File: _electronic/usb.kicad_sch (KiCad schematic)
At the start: 8 parts

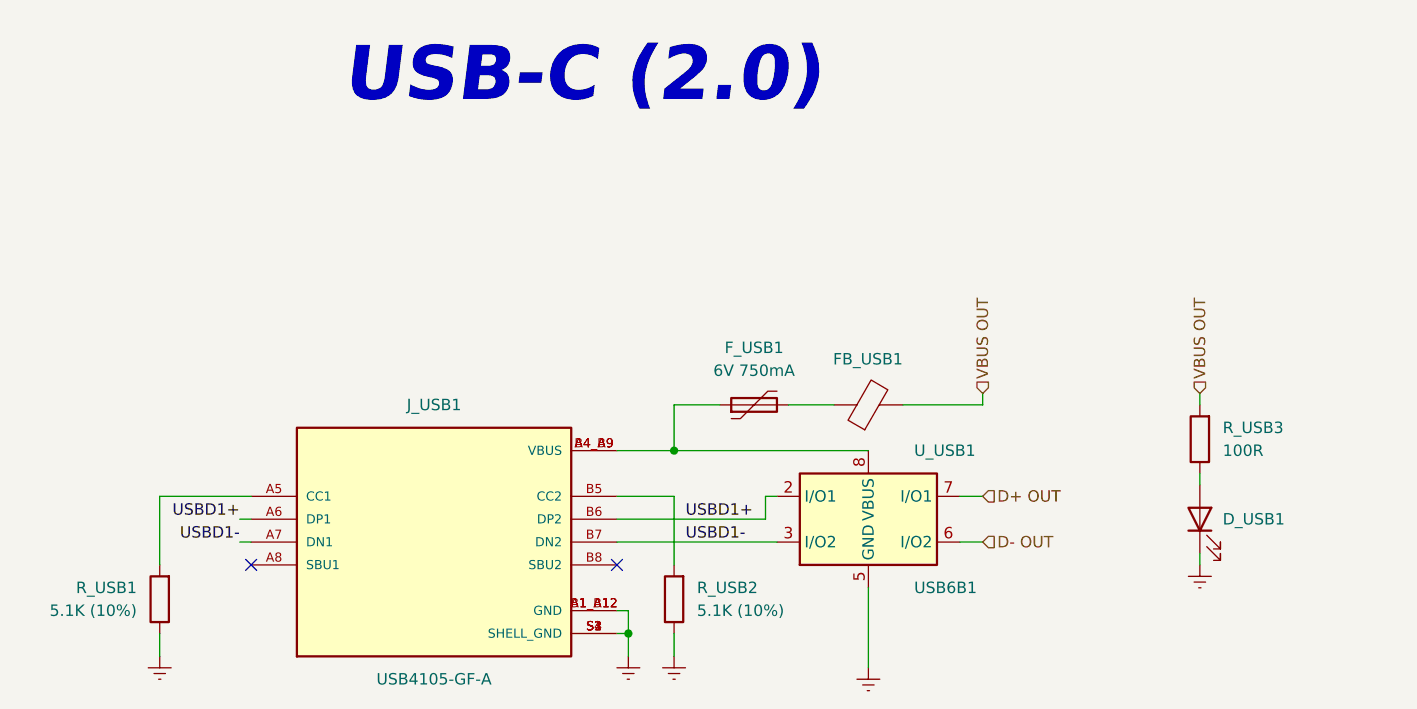
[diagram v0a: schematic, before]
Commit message: led resistor revision, b.o.m. and pcb anotation
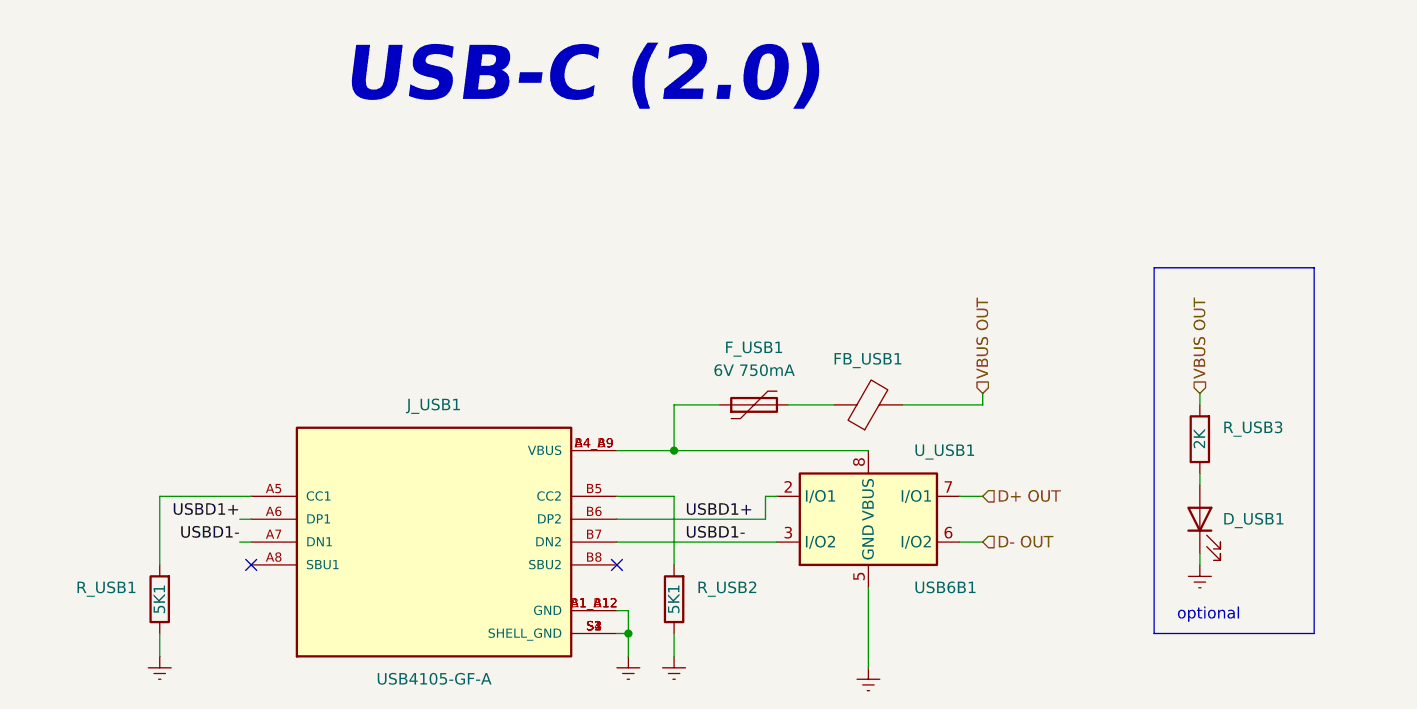
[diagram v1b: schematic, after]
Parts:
- R_USB1, R_USB2: value 5.1K (10%) -> 5K1; # CR0603-FX-5101ELF -> ERJ-3EKF5101V
- R_USB3: value 100R -> 2K; # CHP0603AFX-1000ELF -> ERJ-3EKF2001V
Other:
- note added: "optional"
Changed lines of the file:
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@@
+    (stroke (width 0) (type default) (color 0 0 0 0))
+  )
+  (polyline (pts (xy 201.93 72.39) (xy 219.71 72.39))
     (stroke (width 0) (type default) (color 0 0 0 0))
   )
@@
     (stroke (width 0) (type default) (color 0 0 0 0))
   )
+  (polyline (pts (xy 219.71 72.39) (xy 219.71 113.03))
+    (stroke (width 0) (type default) (color 0 0 0 0))
+  )
   (wire (pts (xy 91.44 97.79) (xy 91.44 105.41))
     (stroke (width 0) (type default) (color 0 0 0 0))
@@
     (stroke (width 0) (type default) (color 0 0 0 0))
   )
+  (polyline (pts (xy 219.71 113.03) (xy 201.93 113.03))
+    (stroke (width 0) (type default) (color 0 0 0 0))
+  )
   (wire (pts (xy 148.59 87.63) (xy 148.59 92.71))
     (stroke (width 0) (type default) (color 0 0 0 0))
@@
   )
   (wire (pts (xy 100.33 102.87) (xy 101.6 102.87))
+    (stroke (width 0) (type default) (color 0 0 0 0))
+  )
+  (polyline (pts (xy 201.93 72.39) (xy 201.93 113.03))
     (stroke (width 0) (type default) (color 0 0 0 0))
   )
@@
     (effects (font (size 6 6) (thickness 0.6) bold italic) (justify left bottom))
   )
+  (text "optional" (at 204.47 111.76 0)
+    (effects (font (size 1.27 1.27)) (justify left bottom))
+  )
   (label "USBD1-" (at 149.86 102.87 0)
     (effects (font (size 1.27 1.27)) (justify left bottom))
@@
       (effects (font (size 1.27 1.27)) (justify right))
     )
-    (property "Value" "5.1K (10%)" (id 1) (at 151.13 110.49 0)
-      (effects (font (size 1.27 1.27)) (justify right))
-    )
+    (property "Value" "5K1" (id 1) (at 148.59 109.22 90))
     (property "Footprint" "Resistor_SMD:R_0603_1608Metric_Pad0.98x0.95mm_HandSolder" (id 2) (at 150.368 109.22 90)
       (effects (font (size 1.27 1.27)) hide)
@@
       (effects (font (size 1.27 1.27)) hide)
     )
-    (property "#" "CR0603-FX-5101ELF" (id 4) (at 151.13 111.76 0)
+    (property "#" "ERJ-3EKF5101V" (id 4) (at 151.13 111.76 0)
       (effects (font (size 1.27 1.27) italic) (justify right) hide)
     )
@@
       (effects (font (size 1.27 1.27)) (justify right))
     )
-    (property "Value" "100R" (id 1) (at 209.55 92.71 0)
-      (effects (font (size 1.27 1.27)) (justify right))
-    )
+    (property "Value" "2K" (id 1) (at 207.01 91.44 90))
     (property "Footprint" "Resistor_SMD:R_0603_1608Metric_Pad0.98x0.95mm_HandSolder" (id 2) (at 208.788 91.44 90)
       (effects (font (size 1.27 1.27)) hide)
@@
       (effects (font (size 1.27 1.27)) hide)
     )
-    (property "#" "CHP0603AFX-1000ELF" (id 4) (at 224.79 90.17 0)
+    (property "#" "ERJ-3EKF2001V" (id 4) (at 224.79 90.17 0)
       (effects (font (size 1.27 1.27) italic) (justify left) hide)
     )
@@
       (effects (font (size 1.27 1.27)) (justify left))
     )
-    (property "Value" "5.1K (10%)" (id 1) (at 88.9 110.49 0)
-      (effects (font (size 1.27 1.27)) (justify left))
-    )
+    (property "Value" "5K1" (id 1) (at 91.44 109.22 90))
     (property "Footprint" "Resistor_SMD:R_0603_1608Metric_Pad0.98x0.95mm_HandSolder" (id 2) (at 93.218 109.22 90)
       (effects (font (size 1.27 1.27)) hide)
@@
       (effects (font (size 1.27 1.27)) hide)
     )
-    (property "#" "CR0603-FX-5101ELF" (id 4) (at 88.9 111.76 0)
+    (property "#" "ERJ-3EKF5101V" (id 4) (at 88.9 111.76 0)
       (effects (font (size 1.27 1.27) italic) (justify left) hide)
     )

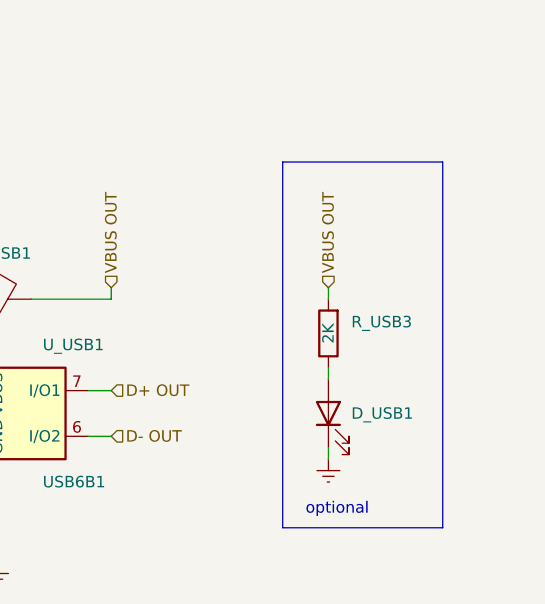
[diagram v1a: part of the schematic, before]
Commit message: schematics and pcb cleanup
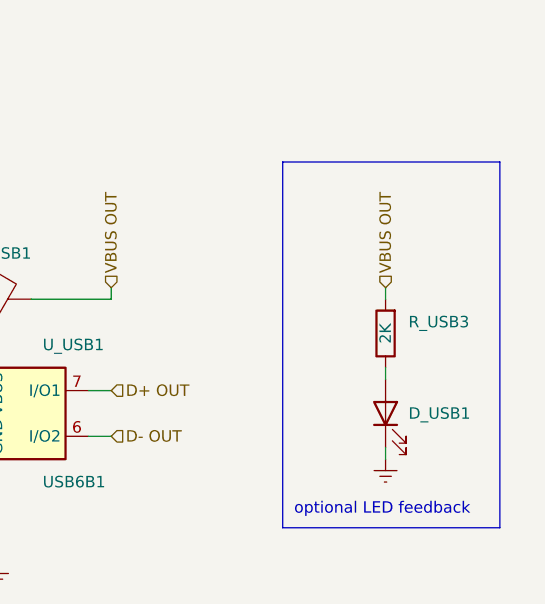
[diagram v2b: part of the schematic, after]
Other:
- note added: "optional LED feedback"
- note removed: "optional"
- title: E-TKT -> E-TKT v1.0
- moved on the sheet: D_USB1, R_USB3
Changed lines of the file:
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@@
   (paper "A4")
   (title_block
-    (title "E-TKT")
-    (date "2022-07-21")
-    (rev "3")
+    (title "E-TKT v1.0")
+    (date "2022-09-29")
+    (rev "4")
     (company "Andrei Speridiao")
   )
@@
     (stroke (width 0) (type default) (color 0 0 0 0))
   )
-  (polyline (pts (xy 201.93 72.39) (xy 219.71 72.39))
+  (polyline (pts (xy 201.93 72.39) (xy 226.06 72.39))
     (stroke (width 0) (type default) (color 0 0 0 0))
   )
@@
     (stroke (width 0) (type default) (color 0 0 0 0))
   )
-  (wire (pts (xy 207.01 104.14) (xy 207.01 105.41))
+  (wire (pts (xy 213.36 104.14) (xy 213.36 105.41))
     (stroke (width 0) (type default) (color 0 0 0 0))
   )
@@
     (stroke (width 0) (type default) (color 0 0 0 0))
   )
-  (polyline (pts (xy 219.71 72.39) (xy 219.71 113.03))
+  (polyline (pts (xy 226.06 72.39) (xy 226.06 113.03))
     (stroke (width 0) (type default) (color 0 0 0 0))
   )
@@
     (stroke (width 0) (type default) (color 0 0 0 0))
   )
-  (polyline (pts (xy 219.71 113.03) (xy 201.93 113.03))
+  (polyline (pts (xy 226.06 113.03) (xy 201.93 113.03))
     (stroke (width 0) (type default) (color 0 0 0 0))
   )
@@
     (stroke (width 0) (type default) (color 0 0 0 0))
   )
-  (wire (pts (xy 207.01 86.36) (xy 207.01 87.63))
+  (wire (pts (xy 213.36 86.36) (xy 213.36 87.63))
     (stroke (width 0) (type default) (color 0 0 0 0))
   )
@@
     (stroke (width 0) (type default) (color 0 0 0 0))
   )
-  (wire (pts (xy 207.01 95.25) (xy 207.01 96.52))
+  (wire (pts (xy 213.36 95.25) (xy 213.36 96.52))
     (stroke (width 0) (type default) (color 0 0 0 0))
   )
@@
     (effects (font (size 6 6) (thickness 0.6) bold italic) (justify left bottom))
   )
-  (text "optional" (at 204.47 111.76 0)
+  (text "optional LED feedback" (at 203.2 111.76 0)
     (effects (font (size 1.27 1.27)) (justify left bottom))
   )
@@
     (effects (font (size 1.27 1.27)) (justify left))
   )
-  (hierarchical_label "VBUS OUT" (shape input) (at 207.01 86.36 90)
+  (hierarchical_label "VBUS OUT" (shape input) (at 213.36 86.36 90)
     (effects (font (size 1.27 1.27)) (justify left))
   )
@@
     (pin "2")
   )
-  (symbol (lib_id "Device:LED") (at 207.01 100.33 90) (unit 1)
+  (symbol (lib_id "Device:LED") (at 213.36 100.33 90) (unit 1)
     (in_bom yes) (on_board yes)
-    (property "Reference" "D_USB1" (id 0) (at 209.55 100.33 90)
+    (property "Reference" "D_USB1" (id 0) (at 215.9 100.33 90)
       (effects (font (size 1.27 1.27)) (justify right))
     )
-    (property "Value" "LED white" (id 1) (at 210.82 102.87 90)
+    (property "Value" "LED white" (id 1) (at 217.17 102.87 90)
       (effects (font (size 1.27 1.27)) (justify right) hide)
     )
-    (property "Footprint" "LED_SMD:LED_0603_1608Metric_Pad1.05x0.95mm_HandSolder" (id 2) (at 207.01 100.33 0)
-      (effects (font (size 1.27 1.27)) hide)
-    )
-    (property "Datasheet" "https://br.mouser.com/datasheet/2/348/smld12-e-1874545.pdf" (id 3) (at 207.01 100.33 0)
-      (effects (font (size 1.27 1.27)) hide)
-    )
-    (property "#" "SMLD12WBN1W1" (id 4) (at 240.03 99.06 90)
+    (property "Footprint" "LED_SMD:LED_0603_1608Metric_Pad1.05x0.95mm_HandSolder" (id 2) (at 213.36 100.33 0)
+      (effects (font (size 1.27 1.27)) hide)
+    )
+    (property "Datasheet" "https://br.mouser.com/datasheet/2/348/smld12-e-1874545.pdf" (id 3) (at 213.36 100.33 0)
+      (effects (font (size 1.27 1.27)) hide)
+    )
+    (property "#" "SMLD12WBN1W1" (id 4) (at 246.38 99.06 90)
       (effects (font (size 1.27 1.27) italic) (justify left) hide)
     )
-    (property "Description" "USB-C power LED" (id 5) (at 207.01 100.33 90)
-      (effects (font (size 1.27 1.27)) hide)
-    )
-    (property "Group" "USB-C" (id 6) (at 207.01 100.33 90)
-      (effects (font (size 1.27 1.27)) hide)
-    )
-    (property "Mouser" "OK" (id 7) (at 207.01 100.33 0)
+    (property "Description" "USB-C power LED" (id 5) (at 213.36 100.33 90)
+      (effects (font (size 1.27 1.27)) hide)
+    )
+    (property "Group" "USB-C" (id 6) (at 213.36 100.33 90)
+      (effects (font (size 1.27 1.27)) hide)
+    )
+    (property "Mouser" "OK" (id 7) (at 213.36 100.33 0)
       (effects (font (size 1.27 1.27)) hide)
     )
@@
     (pin "2")
   )
-  (symbol (lib_id "power:GNDREF") (at 207.01 105.41 0) (unit 1)
-    (in_bom yes) (on_board yes) (fields_autoplaced)
-    (property "Reference" "#PWR0155" (id 0) (at 207.01 111.76 0)
-      (effects (font (size 1.27 1.27)) hide)
-    )
-    (property "Value" "GNDREF" (id 1) (at 207.01 110.49 0)
-      (effects (font (size 1.27 1.27)) hide)
-    )
-    (property "Footprint" "" (id 2) (at 207.01 105.41 0)
-      (effects (font (size 1.27 1.27)) hide)
-    )
-    (property "Datasheet" "" (id 3) (at 207.01 105.41 0)
+  (symbol (lib_id "power:GNDREF") (at 213.36 105.41 0) (unit 1)
+    (in_bom yes) (on_board yes) (fields_autoplaced)
+    (property "Reference" "#PWR0155" (id 0) (at 213.36 111.76 0)
+      (effects (font (size 1.27 1.27)) hide)
+    )
+    (property "Value" "GNDREF" (id 1) (at 213.36 110.49 0)
+      (effects (font (size 1.27 1.27)) hide)
+    )
+    (property "Footprint" "" (id 2) (at 213.36 105.41 0)
+      (effects (font (size 1.27 1.27)) hide)
+    )
+    (property "Datasheet" "" (id 3) (at 213.36 105.41 0)
       (effects (font (size 1.27 1.27)) hide)
     )
@@
     (pin "1")
   )
-  (symbol (lib_id "Device:R") (at 207.01 91.44 180) (unit 1)
+  (symbol (lib_id "Device:R") (at 213.36 91.44 180) (unit 1)
     (in_bom yes) (on_board yes)
-    (property "Reference" "R_USB3" (id 0) (at 209.55 90.17 0)
+    (property "Reference" "R_USB3" (id 0) (at 215.9 90.17 0)
       (effects (font (size 1.27 1.27)) (justify right))
     )
-    (property "Value" "2K" (id 1) (at 207.01 91.44 90))
-    (property "Footprint" "Resistor_SMD:R_0603_1608Metric_Pad0.98x0.95mm_HandSolder" (id 2) (at 208.788 91.44 90)
-      (effects (font (size 1.27 1.27)) hide)
-    )
-    (property "Datasheet" "https://br.mouser.com/datasheet/2/54/chp_a-1858677.pdf" (id 3) (at 207.01 91.44 0)
-      (effects (font (size 1.27 1.27)) hide)
-    )
-    (property "#" "ERJ-3EKF2001V" (id 4) (at 224.79 90.17 0)
+    (property "Value" "2K" (id 1) (at 213.36 91.44 90))
+    (property "Footprint" "Resistor_SMD:R_0603_1608Metric_Pad0.98x0.95mm_HandSolder" (id 2) (at 215.138 91.44 90)
+      (effects (font (size 1.27 1.27)) hide)
+    )
+    (property "Datasheet" "https://br.mouser.com/datasheet/2/54/chp_a-1858677.pdf" (id 3) (at 213.36 91.44 0)
+      (effects (font (size 1.27 1.27)) hide)
+    )
+    (property "#" "ERJ-3EKF2001V" (id 4) (at 231.14 90.17 0)
       (effects (font (size 1.27 1.27) italic) (justify left) hide)
     )
-    (property "Description" "USB-C power LED resistor" (id 5) (at 207.01 91.44 0)
-      (effects (font (size 1.27 1.27)) hide)
-    )
-    (property "Group" "USB-C" (id 6) (at 207.01 91.44 0)
-      (effects (font (size 1.27 1.27)) hide)
-    )
-    (property "Obs" "wes" (id 7) (at 207.01 91.44 0)
-      (effects (font (size 1.27 1.27)) hide)
-    )
-    (property "Mouser" "OK" (id 8) (at 207.01 91.44 0)
-      (effects (font (size 1.27 1.27)) hide)
-    )
+    (property "Description" "USB-C power LED resistor" (id 5) (at 213.36 91.44 0)
+      (effects (font (size 1.27 1.27)) hide)
+    )
+    (property "Group" "USB-C" (id 6) (at 213.36 91.44 0)
+      (effects (font (size 1.27 1.27)) hide)
+    )
+    (property "Obs" "wes" (id 7) (at 213.36 91.44 0)
+      (effects (font (size 1.27 1.27)) hide)
+    )
+    (property "Mouser" "OK" (id 8) (at 213.36 91.44 0)
+      (effects (font (size 1.27 1.27)) hide)
+    )
